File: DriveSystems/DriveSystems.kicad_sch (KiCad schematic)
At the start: 22 parts, among them J1 Raspberry_Pi_4, M1 Motor_Servo, M2 Motor_Servo, SW1 SW_Rotary_1x2_MP, U1 RoboClaw Motor Controller, U2 5304 Gear Motor, U3 24VDC UBC-C PSU, U4 24V 5V10A DCDC Stepdown, U5 RoboClaw VClamp, U6 Pwr Res

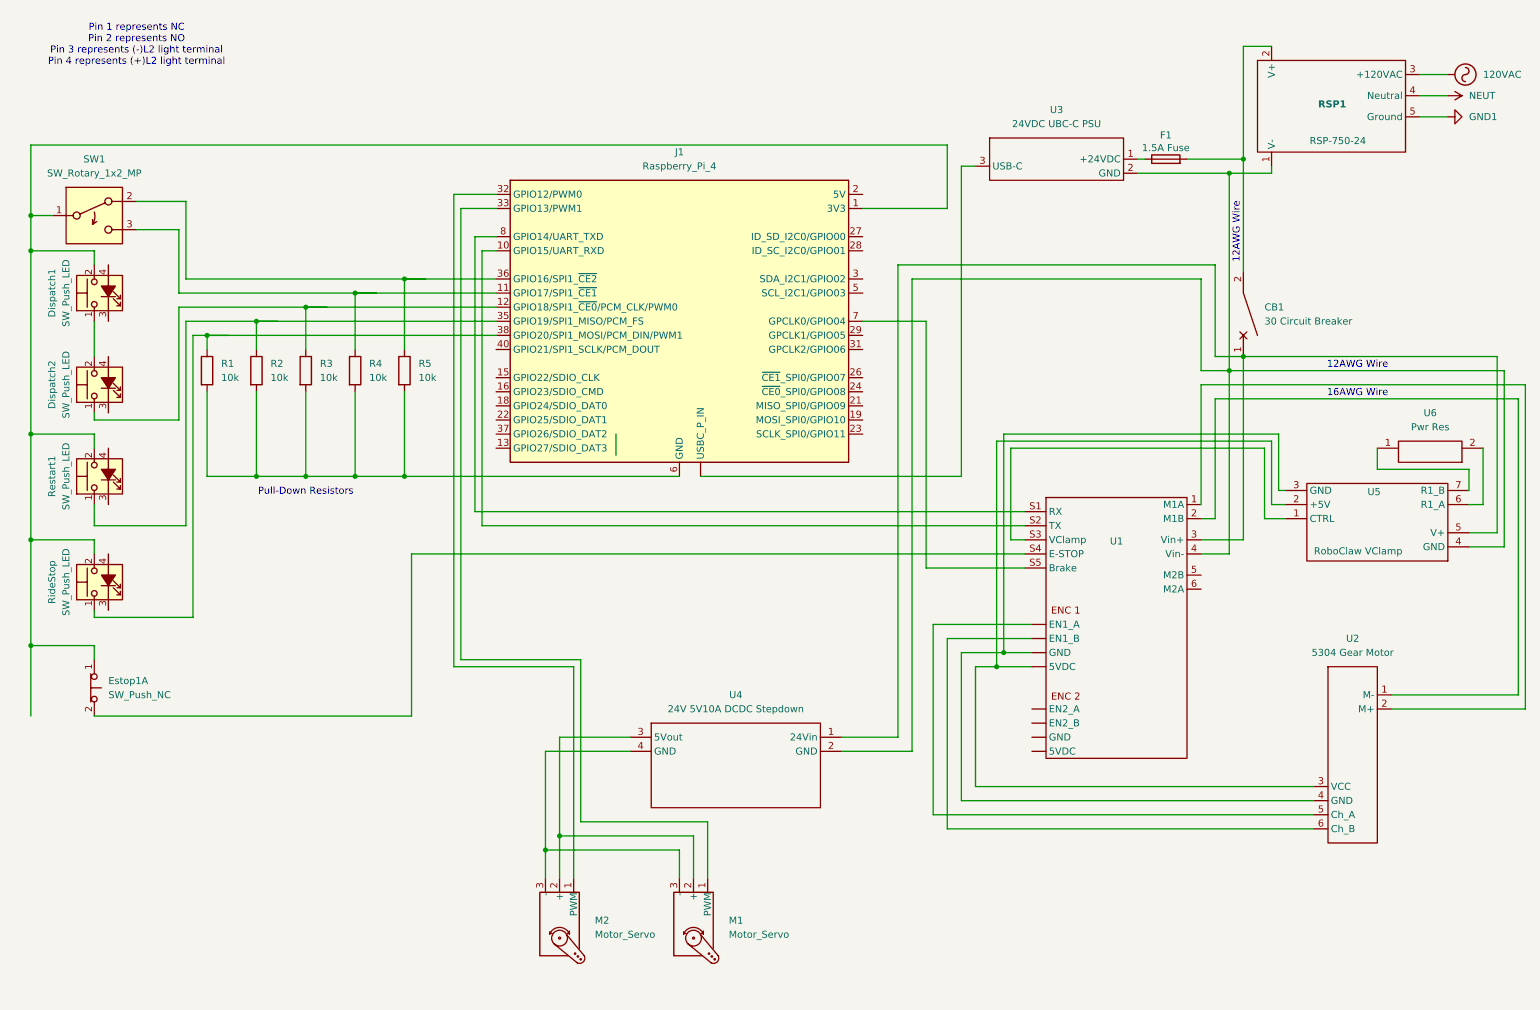
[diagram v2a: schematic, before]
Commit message: Added RCP Firewall
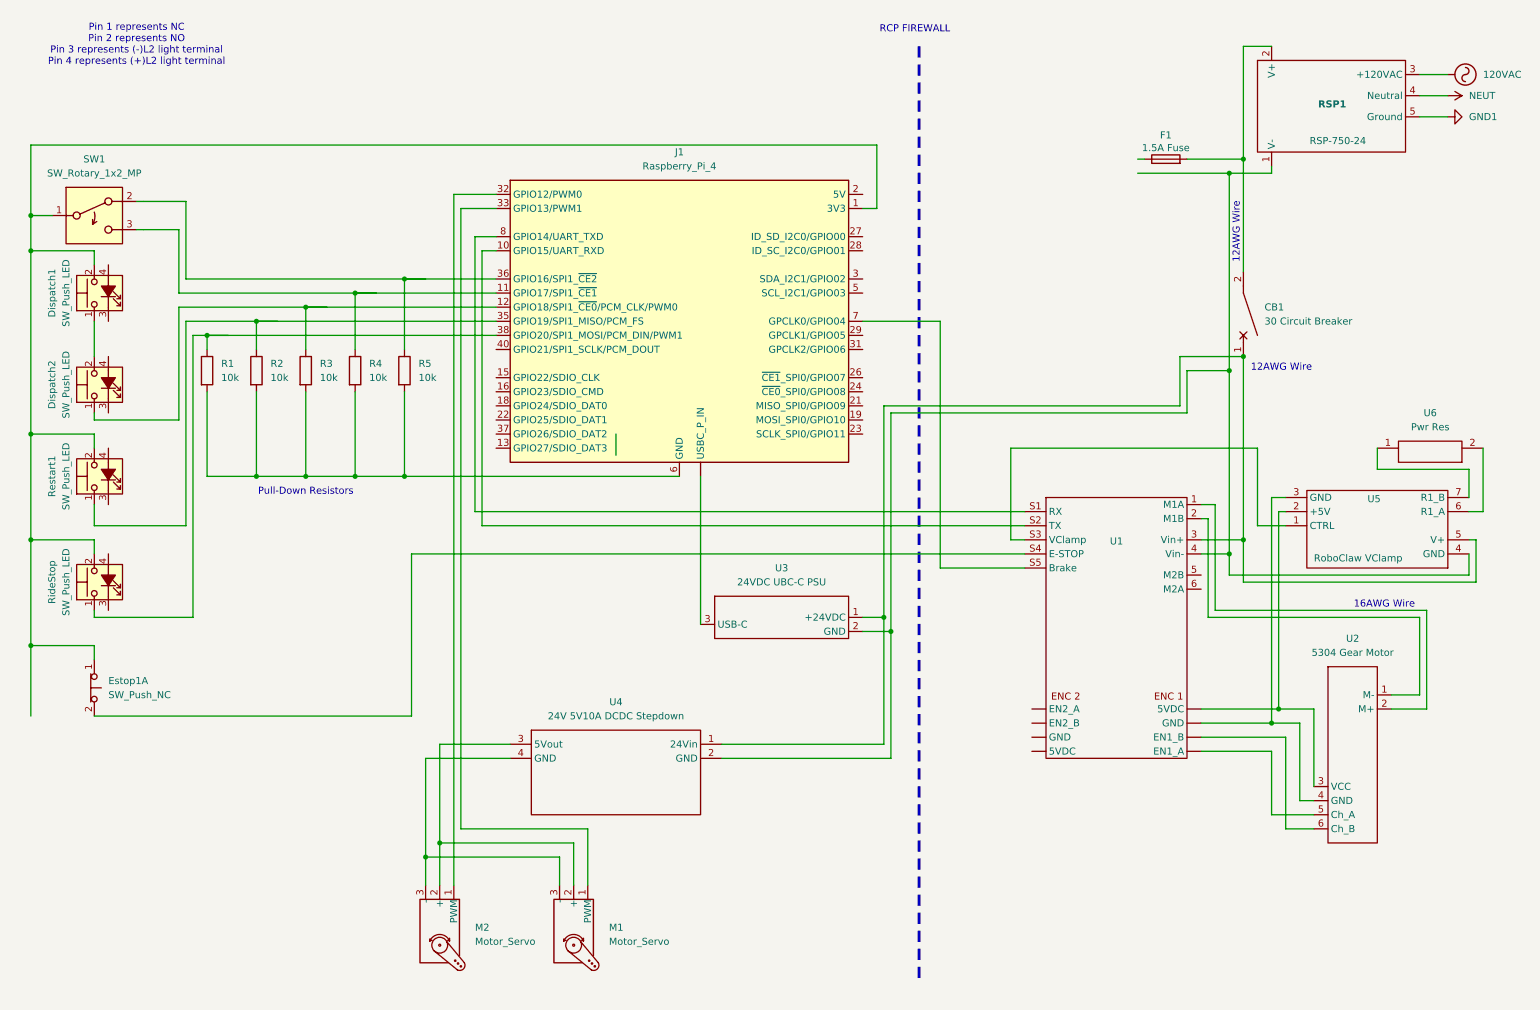
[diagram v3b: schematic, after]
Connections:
- net at U1. (EN1_A): now also U2.6 (Ch_B)
- net at CB1.1, U1.3 (Vin+), U4.1 (24Vin)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: now also U3.1 (+24VDC)
- net at F1.1: no longer U3.1 (+24VDC)
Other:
- note added: "RCP FIREWALL"
- moved on the sheet: M1, M2, U3, U4, U5

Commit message: Update DriveSystems.kicad_sch
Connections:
- net at U1. (EN1_A): now also U2.6 (Ch_B)
- net at CB1.1, U1.3 (Vin+), U4.1 (24Vin)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: now also F1.2; no longer U3.1 (+24VDC)
- net at F1.1: now also U3.1 (+24VDC)
- net at CB1.2: no longer F1.2
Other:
- moved on the sheet: F1, U3

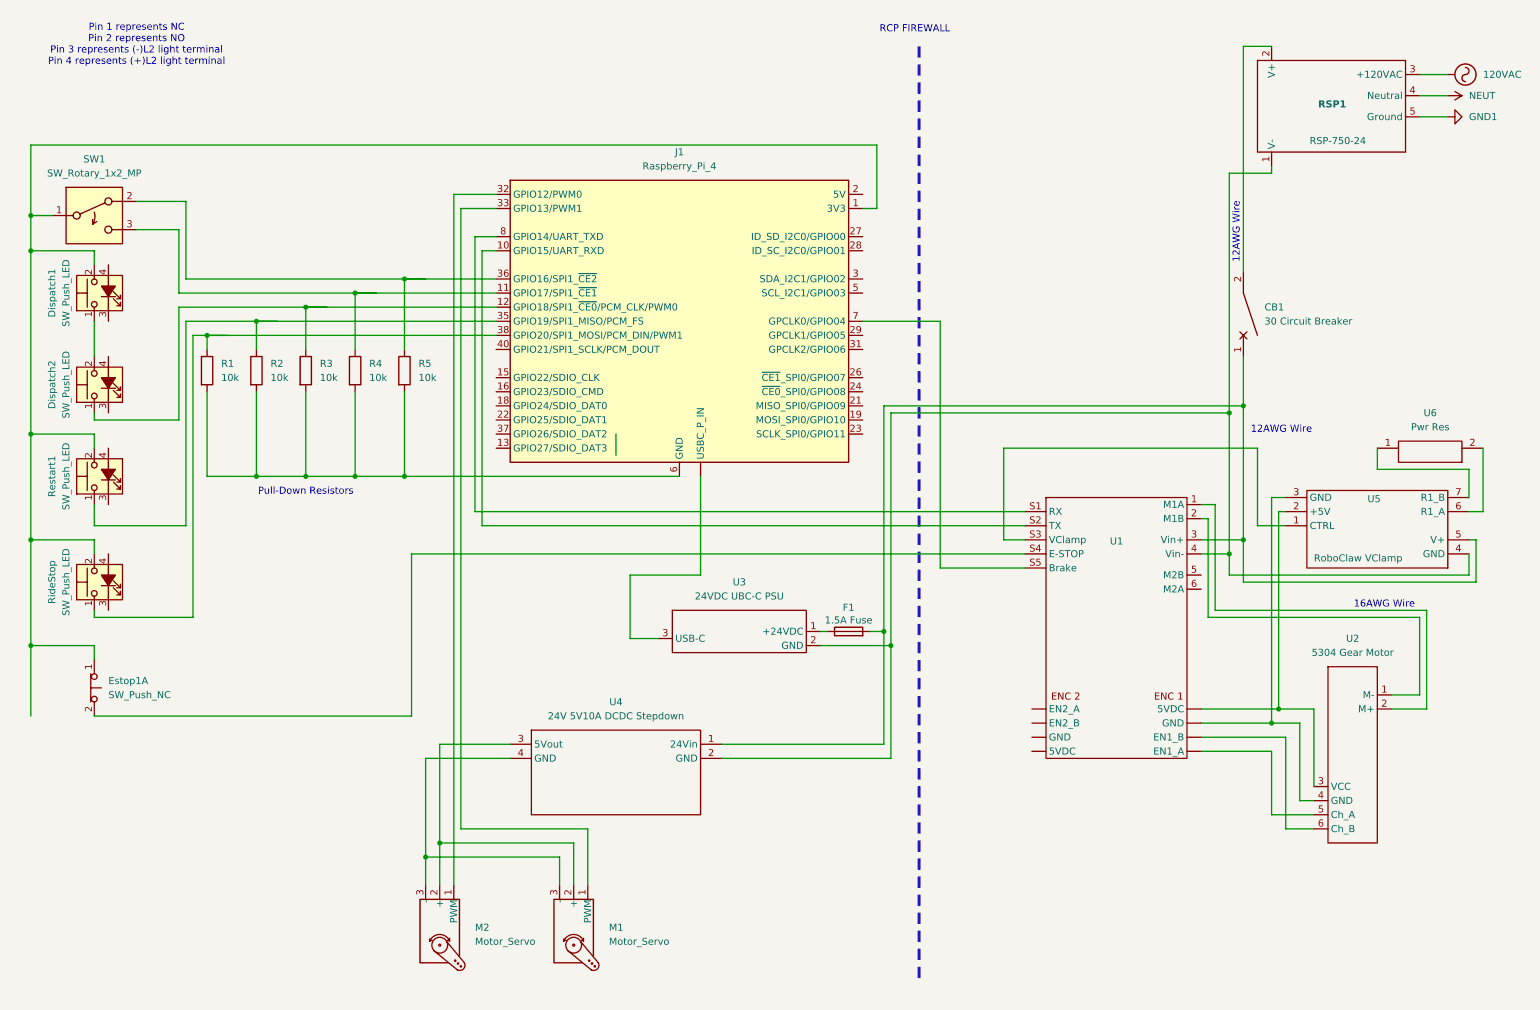
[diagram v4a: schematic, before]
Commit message: Properly fused things
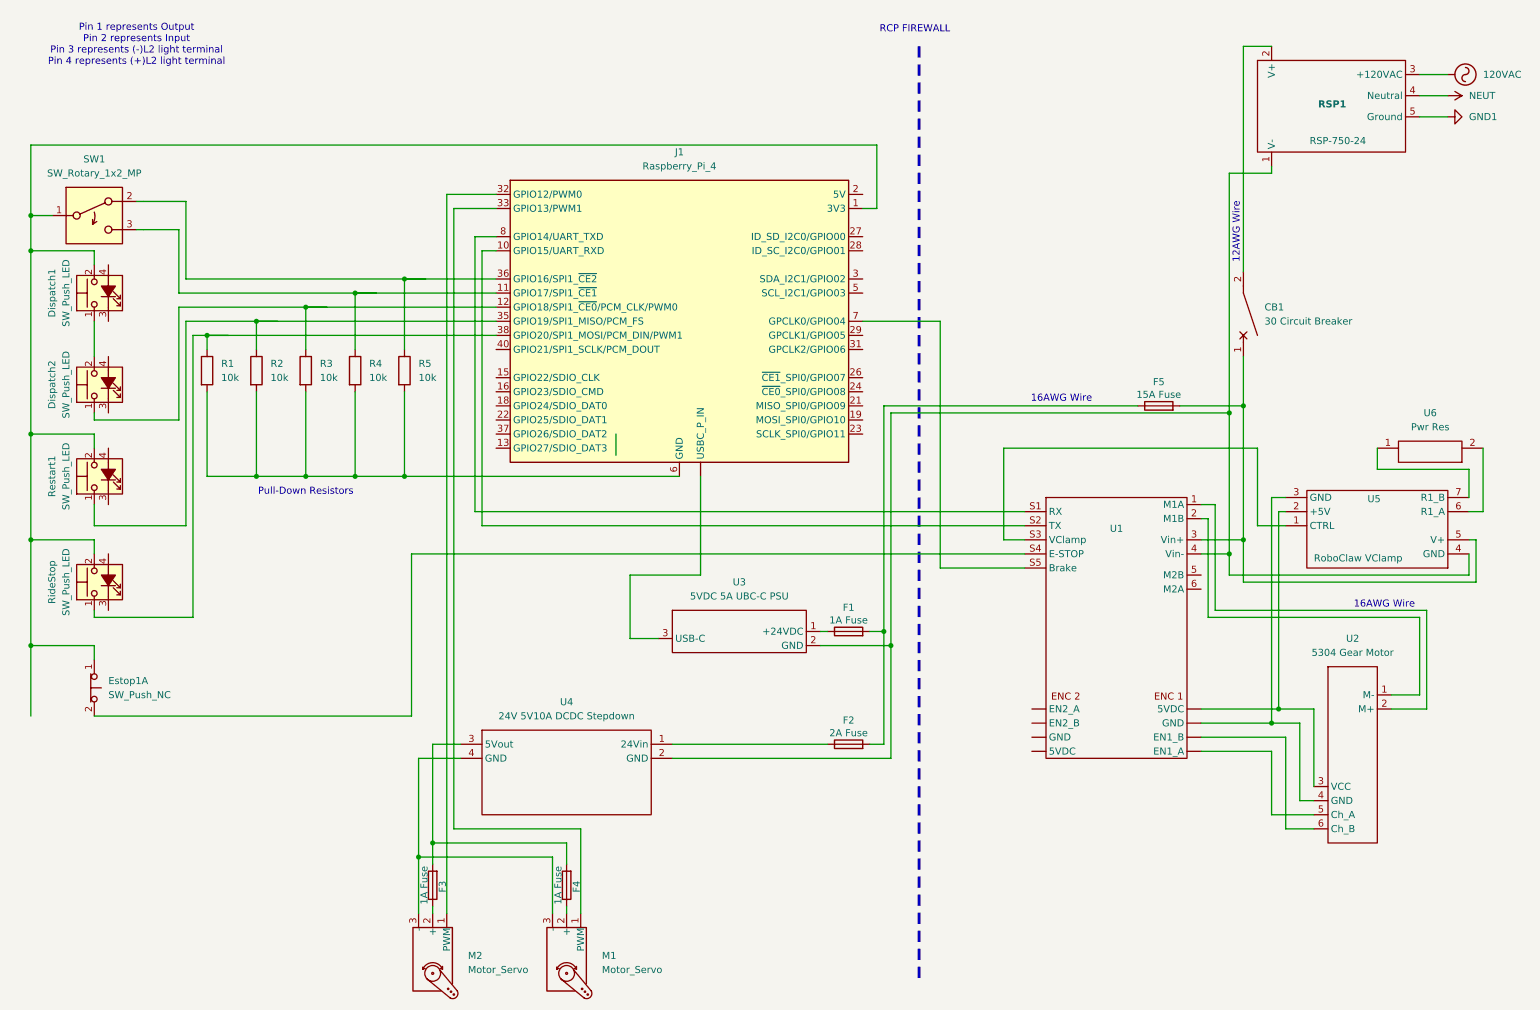
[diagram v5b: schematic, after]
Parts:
- added F2: 2A Fuse, symbol Device:Fuse
- added F3, F4: 1A Fuse, symbol Device:Fuse
- added F5: 15A Fuse, symbol Device:Fuse
- F1: value 1.5A Fuse -> 1A Fuse
- U3: value 24VDC UBC-C PSU -> 5VDC 5A UBC-C PSU
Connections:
- net at U1. (EN1_A): now also U2.6 (Ch_B)
- net at CB1.1, U1.3 (Vin+), U5.5 (V+): now also F5.2; no longer F1.2, U4.1 (24Vin)
- new net: F2.1, U4.1 (24Vin)
- new net: F1.2, F2.2, F5.1
- new net: F3.2, F4.2, U4.3 (5Vout)
- new net: F3.1, M2.2 (+)
- new net: F4.1, M1.2 (+)
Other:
- note added: "Pin 1 represents Output Pin 2 represents Input Pin 3 represents (-)L2 light terminal Pin 4 represents (+)L2 light terminal"
- note removed: "Pin 1 represents NC Pin 2 represents NO Pin 3 represents (-)L2 light terminal Pin 4 represents (+)L2 light terminal"
- moved on the sheet: M1, M2, U4

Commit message: Final Revision
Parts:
- added R6: 1k, symbol Device:R
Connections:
- net at Dispatch1.2, J1.1 (3V3), J1.17 (3V3)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: now also Estop1.2; no longer Estop1.1
- net at U1. (EN1_A): now also R6.2
- net at U1.S4 (E-STOP): now also Estop1.1, R6.1; no longer Estop1.2
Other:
- moved on the sheet: Estop1A, F2, U4

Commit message: Added LED Tape (Rev F)
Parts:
- added F6: 2A Fuse, symbol Device:Fuse
- added U7: ~, symbol CustomSymbols:24V_LED_Tape
- CB1: value 30 Circuit Breaker -> 30A Circuit Breaker
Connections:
- net at U1. (EN1_A): now also R6.2
- net at U1.4 (Vin-), U3.2 (GND), U4.2 (GND)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: now also U7.2 (GND)
- net at F1.2, F2.2, F5.1: now also F6.2
- new net: F6.1, U7.1 (+24V)
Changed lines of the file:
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@@
 		(title "REC 2025 ELECTRONIC SCHEMATIC")
 		(date "2025-03-04")
-		(rev "E")
+		(rev "F")
 		(company "TERRIER RIDE ENGINEERING CLUB")
 		(comment 1 "FINAL")
@@
 	(text "16AWG Wire"
 		(exclude_from_sim no)
-		(at 200.914 83.82 0)
+		(at 189.484 83.566 0)
 		(effects
 			(font
@@
 	)
 	(junction
+		(at 203.2 86.36)
+		(diameter 0)
+		(color 0 0 0 0)
+	)
+	(junction
 		(at 231.14 86.36)
 		(diameter 0)
@@
 	)
 	(junction
+		(at 205.74 85.09)
+		(diameter 0)
+		(color 0 0 0 0)
+	)
+	(junction
 		(at 238.76 142.24)
 		(diameter 0)
@@
 	(wire
 		(pts
+			(xy 203.2 69.85) (xy 203.2 86.36)
+		)
+		(stroke
+			(width 0)
+			(type default)
+		)
+	)
+	(wire
+		(pts
 			(xy 238.76 101.6) (xy 241.3 101.6)
 		)
@@
 	(wire
 		(pts
+			(xy 205.74 85.09) (xy 214.63 85.09)
+		)
+		(stroke
+			(width 0)
+			(type default)
+		)
+	)
+	(wire
+		(pts
 			(xy 179.07 69.85) (xy 165.1 69.85)
 		)
@@
 	(wire
 		(pts
-			(xy 184.15 85.09) (xy 214.63 85.09)
+			(xy 184.15 85.09) (xy 205.74 85.09)
 		)
 		(stroke
@@
 	(wire
 		(pts
+			(xy 205.74 69.85) (xy 205.74 73.66)
+		)
+		(stroke
+			(width 0)
+			(type default)
+		)
+	)
+	(wire
+		(pts
 			(xy 26.67 92.71) (xy 26.67 90.17)
 		)
@@
 	(wire
 		(pts
-			(xy 185.42 86.36) (xy 231.14 86.36)
+			(xy 185.42 86.36) (xy 203.2 86.36)
+		)
+		(stroke
+			(width 0)
+			(type default)
+		)
+	)
+	(wire
+		(pts
+			(xy 203.2 86.36) (xy 231.14 86.36)
+		)
+		(stroke
+			(width 0)
+			(type default)
+		)
+	)
+	(wire
+		(pts
+			(xy 205.74 81.28) (xy 205.74 85.09)
 		)
 		(stroke
@@
 			)
 		)
-		(property "Value" "30 Circuit Breaker"
+		(property "Value" "30A Circuit Breaker"
 			(at 237.49 69.8499 0)
 			(effects
@@
 	)
 	(symbol
+		(lib_id "Device:Fuse")
+		(at 205.74 77.47 0)
+		(unit 1)
+		(exclude_from_sim no)
+		(in_bom yes)
+		(on_board yes)
+		(dnp no)
+		(property "Reference" "F6"
+			(at 210.058 77.47 90)
+			(effects
+				(font
+					(size 1.27 1.27)
+				)
+			)
+		)
+		(property "Value" "2A Fuse"
+			(at 207.772 77.47 90)
+			(effects
+				(font
+					(size 1.27 1.27)
+				)
+			)
+		)
+		(property "Footprint" ""
+			(at 203.962 77.47 90)
+			(effects
+				(font
+					(size 1.27 1.27)
+				)
+				(hide yes)
+			)
+		)
+		(property "Datasheet" "~"
+			(at 205.74 77.47 0)
+			(effects
+				(font
+					(size 1.27 1.27)
+				)
+				(hide yes)
+			)
+		)
+		(property "Description" "Fuse"
+			(at 205.74 77.47 0)
+			(effects
+				(font
+					(size 1.27 1.27)
+				)
+				(hide yes)
+			)
+		)
+		(pin "1"
+		)
+		(pin "2"
+		)
+		(instances
+			(project "DriveSystems"
+				(path "/09f307af-601f-4645-b594-daaafb49fd2a"
+					(reference "F6")
+					(unit 1)
+				)
+			)
+		)
+	)
+	(symbol
 		(lib_id "Switch:SW_Rotary_1x3_MP")
 		(at 26.67 50.8 0)
@@
 					(unit 1)
 				)
+			)
+		)
+	)
+	(symbol
+		(lib_id "CustomSymbols:24V_LED_Tape")
+		(at 203.2 50.8 0)
+		(unit 1)
+		(exclude_from_sim no)
+		(in_bom yes)
+		(on_board yes)
+		(dnp no)
+		(property "Reference" "U7"
+			(at 212.598 65.278 0)
+			(effects
+				(font
+					(size 1.27 1.27)
+				)
+				(justify left)
+			)
+		)
+		(property "Value" "~"
+			(at 217.17 59.055 0)
+			(effects
+				(font
+					(size 1.27 1.27)
+				)
+				(justify left)
+			)
+		)
+		(property "Footprint" ""
+			(at 203.2 50.8 0)
+			(effects
+				(font
+					(size 1.27 1.27)
+				)
+				(hide yes)
+			)
+		)
+		(property "Datasheet" ""
+			(at 203.2 50.8 0)
+			(effects
+				(font
+					(size 1.27 1.27)
+				)
+				(hide yes)
+			)
+		)
+		(property "Description" ""
+			(at 203.2 50.8 0)
+			(effects
+				(font
+					(size 1.27 1.27)
+				)
+				(hide yes)
+			)
+		)
+		(pin "1"
+		)
+		(pin "2"
+		)
+		(instances
+			(project ""
+				(path "/09f307af-601f-4645-b594-daaafb49fd2a"
+					(reference "U7")
+					(unit 1)
+				)
